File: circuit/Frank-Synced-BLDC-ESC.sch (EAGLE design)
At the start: 57 parts, among them IC1 Vreg +5V, Q1 PMOS-DPAK, Q2 NMOS-DPAK, Q4 PMOS-DPAK, Q5 NMOS-DPAK, Q7 PMOS-DPAK, Q8 NMOS-DPAK, U1 ATMEGA168MLF, U2 OSC-16MHz

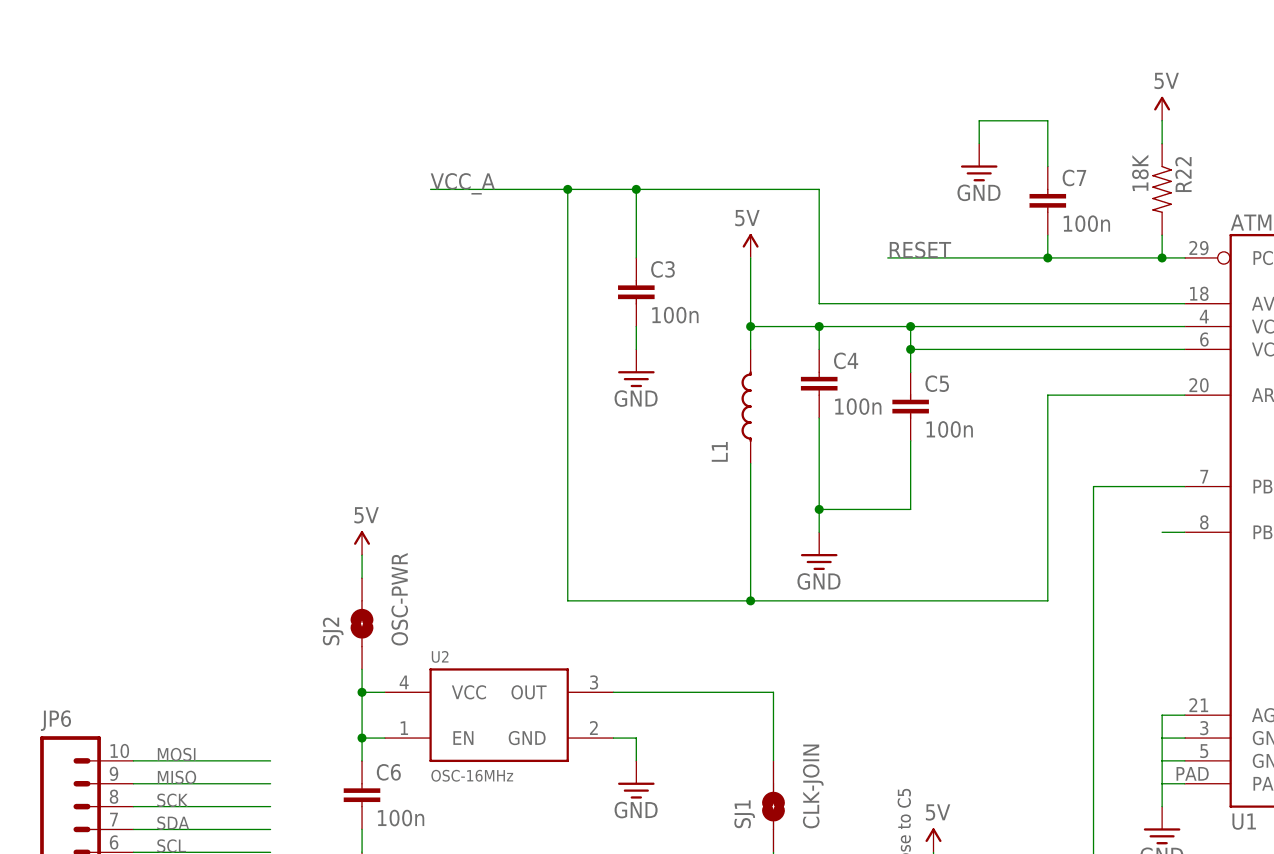
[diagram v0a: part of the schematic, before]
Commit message: branch uses 2.5 x 2 mm sized +3.3V powered oscillator instead
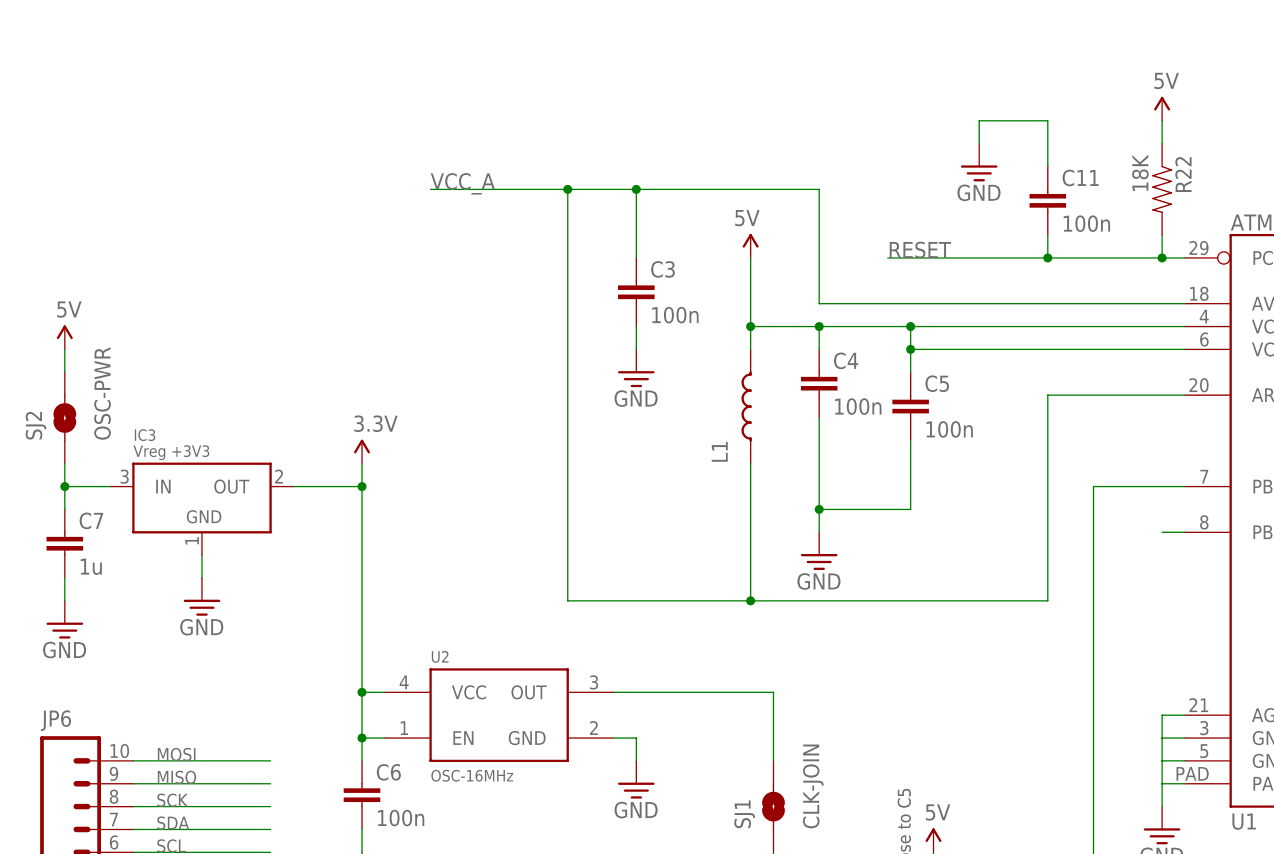
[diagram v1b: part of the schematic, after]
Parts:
- added C11: 100n, Frank-Synced-BLDC-ESC:CAP0603-CAP
- added IC3: Vreg +3V3, Frank-Synced-BLDC-ESC:V_REG_LDO-SOT23-3
- C7: value 100n -> 1u
- U2: device Frank-Synced-BLDC-ESC:OSCILLATOR5X3-PIN1-INDICATED -> Frank-Synced-BLDC-ESC:OSCILLATOR-2.5X2
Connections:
- removed net N$25: C6.1, SJ2.1, U2.EN, U2.VCC
- new net 3.3V: C6.1, IC3.OUT, U2.EN, U2.VCC
- new net N$9: C7.1, IC3.IN, SJ2.1
- net GND: now also C11.1, C7.2, IC3.GND; no longer C7.1
- net RESET: now also C11.2; no longer C7.2
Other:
- moved on the sheet: C7, SJ2
